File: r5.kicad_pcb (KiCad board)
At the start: 4 copper layers, 94.4 x 92.2 mm, 81 parts, among them SW10 SW_SPDT, SW60 SW_SPDT, SW70 SW_SPDT, SW80 SW_SPDT, U10 LMZ22005, U20 DRV8871DDA, U21 DRV8871DDA, U22 DRV8871DDA, U23 DRV8871DDA, U24 DRV8871DDA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

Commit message: routing done
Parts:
- added G***: LOGO, LOGO, B.Cu at (99.7, 95.1)
- R10: value 102k -> 22k
- R11: value 13k7 -> 3k
- moved R10 16.2 mm to (108.0, 122.6), turned to 90 degrees
- moved R16 15.3 mm to (109.9, 122.6), turned to 90 degrees
- moved R17 15.2 mm to (109.9, 119.2), turned to -90 degrees
- moved R11 14.4 mm to (106.1, 122.6), turned to -90 degrees
- moved R12 13.3 mm to (104.2, 122.6), turned to -90 degrees
- moved R13 13.2 mm to (104.2, 119.2), turned to 90 degrees
- moved C10 12.9 mm to (105.6, 125.5), turned to 0 degrees
- moved R15 12.7 mm to (108.0, 119.2), turned to -90 degrees
- moved R14 11.7 mm to (106.1, 119.2), turned to 90 degrees
- moved R90 9.80 mm to (111.0, 70.3), turned to 90 degrees
- moved U10 9.65 mm to (101.3, 122.0), turned to 90 degrees
- moved NT50 9.18 mm to (94.3, 128.0), turned to -90 degrees
- moved C11 5.77 mm to (104.1, 113.9), turned to 0 degrees
- moved R60 5.00 mm to (94.5, 68.7)
- moved S60 4.70 mm to (94.2, 60.9)
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- renumbered SW10 to S10, SW60 to S60, SW70 to S70, SW80 to S80
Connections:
- X10 pad 1: GND -> GNDPWR
- X11 pad 1: GND -> GNDPWR
- X11 pad 2: GND -> GNDPWR
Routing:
- net GND: track 32.5 -> 143.8 mm, vias 12 -> 36
- net WSLED: track 0.00 -> 74.3 mm
- net PICOTX: track 0.00 -> 72.6 mm, vias 0 -> 1
- net ZERO0: track 0.00 -> 71.6 mm
- net PICORX: track 0.00 -> 68.6 mm, vias 0 -> 1
- net VBATMEASURE: track 0.00 -> 47.2 mm
- net Net-(S70-C): track 26.8 -> 69.4 mm
- net SERVOSDA: track 5.71 -> 47.8 mm, vias 0 -> 1
- net MENABLE: track 1.56 -> 43.2 mm, vias 0 -> 2
- net SERVOSCL: track 8.58 -> 47.2 mm, vias 0 -> 1
- net +5V: track 0.00 -> 37.0 mm, vias 0 -> 7
- net SWCLK: track 0.00 -> 35.3 mm, vias 0 -> 1
- net Net-(D41-DOUT): track 0.00 -> 33.7 mm, vias 0 -> 1
- net SWDIO: track 0.00 -> 30.6 mm, vias 0 -> 1
- net INWIFI: track 0.00 -> 26.4 mm, vias 0 -> 1
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- added copper zone on In2.Cu, net +3.3V
- added copper zone on In2.Cu, net +5V
- added copper zone on F.Cu, net +BATT
- added copper zone on B.Cu, net GND
- added copper zone on In2.Cu, net GND
- added copper zone on B.Cu, net unconnected-(U60-LED14-Pad21)
- added copper zone on In1.Cu, net unconnected-(U60-LED14-Pad21)
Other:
- board text added: "+5V"
- board text added: "1"
- board text added: "Battery +"
- board text added: "Battery -"
- board text added: "Gnd"
- board text added: "R5-PCB Feb. 2024 github.com/dkjonas/WildWillyR5Hardware"
- board text added: "Servos +5V Gnd"
- board text added: "Zeros"
- board text removed: "WildWilly 6-6-2021"

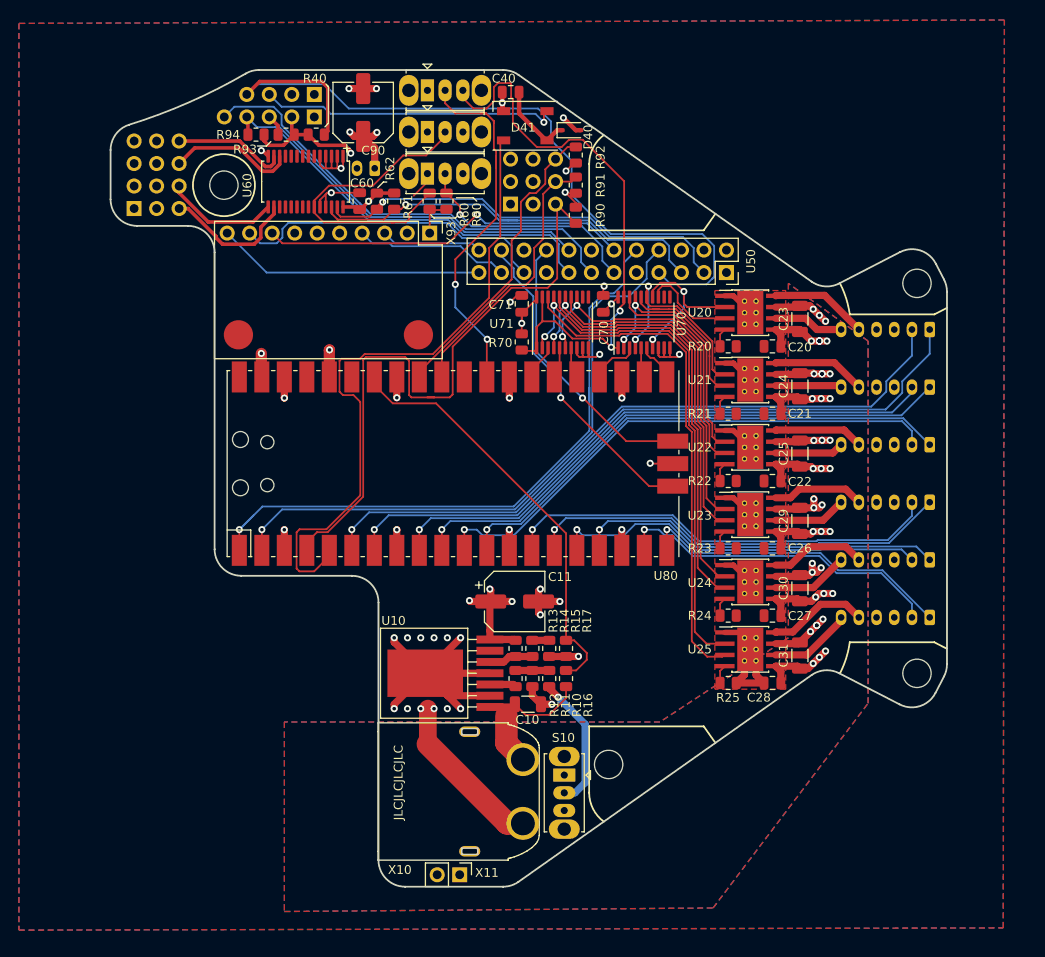
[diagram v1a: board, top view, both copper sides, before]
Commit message: remove some DRC
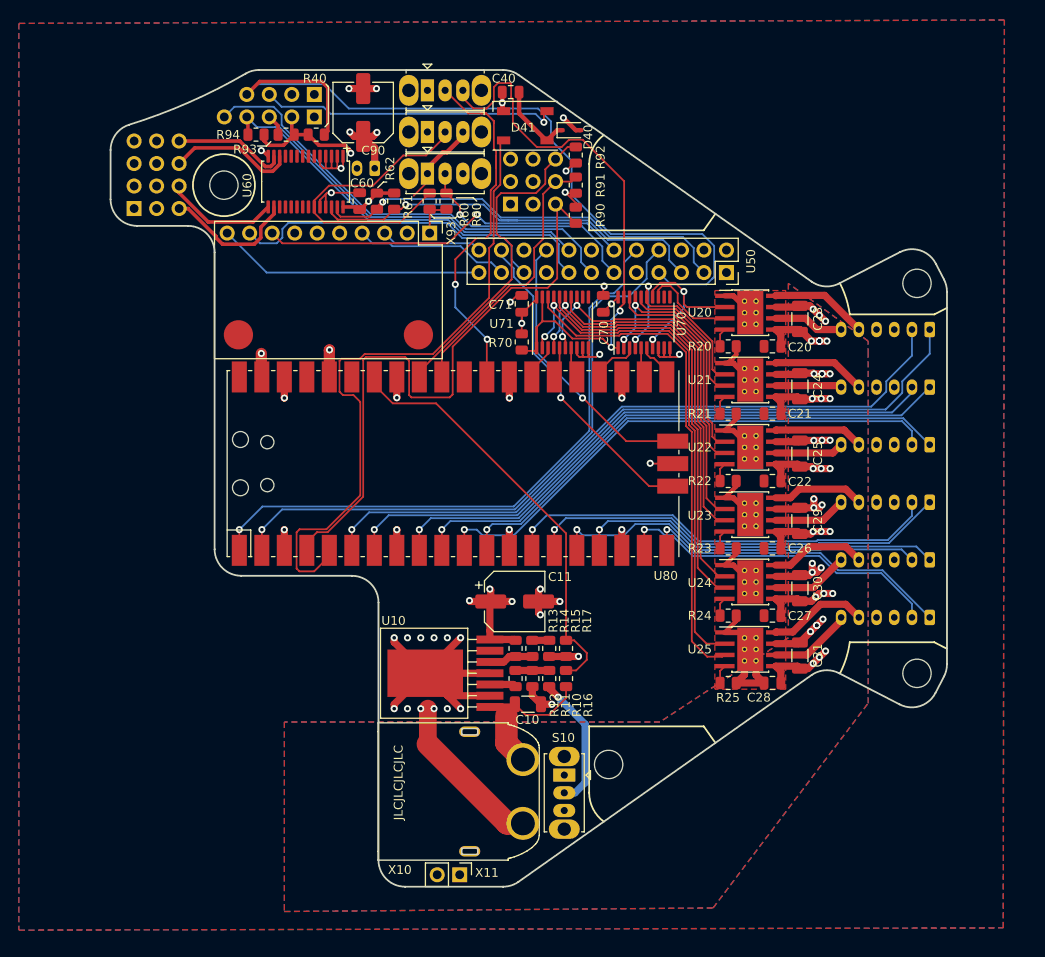
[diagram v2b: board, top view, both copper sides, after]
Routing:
- net GND: track 143.8 -> 206.9 mm
- net +5V: track 37.0 -> 48.1 mm
- net PICOTX: track 72.6 -> 68.8 mm
- net ZERO2: track 35.1 -> 38.7 mm
- net OLEDRES: track 52.6 -> 51.3 mm
- net ZERO0: track 71.6 -> 70.8 mm
- net EM2: track 17.0 -> 16.3 mm
- net Net-(S60-B): track 35.2 -> 34.6 mm
- net E5B: track 41.5 -> 41.0 mm
- added copper zone on B.Cu, net GNDPWR
- removed copper zone on B.Cu, net unconnected-(U60-LED14-Pad21)
- removed copper zone on In1.Cu, net unconnected-(U60-LED14-Pad21)

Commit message: Silk cleanup
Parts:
- moved R80 2.61 mm to (99.0, 68.9), turned to 0 degrees
- moved R60 1.02 mm to (95.5, 68.9), turned to 180 degrees
- moved C40 0.11 mm to (103.6, 56.3)
- moved D41 0.10 mm to (105.3, 60.1)
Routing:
- net INWIFI: track 26.4 -> 28.6 mm
- net +3.3V: track 43.6 -> 44.9 mm

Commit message: board done
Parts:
- U20, U21, U22, U23, U24, U25: footprint Package_SO:Texas_HTSOP-8-1EP_3.9x4.9mm_P1.27mm_EP2.95x4.9mm_Mask2.4x3.1mm_ThermalVias -> _r5:Texas_HTSOP-8-1EP_3.9x4.9mm_P1.27mm_EP2.95x4.9mm_Mask2.4x3.1mm_ThermalVias
- moved X12 0.10 mm to (88.3, 64.9)
- turned C90 to -90 degrees
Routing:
- net GND: track 206.9 -> 204.0 mm, vias 36 -> 64
- net +5V: track 48.1 -> 49.5 mm
- net +BATT: track 69.6 -> 69.7 mm, vias 20 -> 18
- net GNDPWR: vias 20 -> 18
